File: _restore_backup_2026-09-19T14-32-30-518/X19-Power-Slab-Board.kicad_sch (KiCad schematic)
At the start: 33 parts, among them J2 796636-6, J3 Conn_01x02_Pin, J4 Conn_01x04_Pin, J5 Conn_01x04_Pin, Q1 TSM340N06CP_ROG, U2 MIC5504-3.3YM5-TR, U3 INA237AIDGSR, U4 TMP1075NDRLR, U6 TCAN1044AVDRQ1

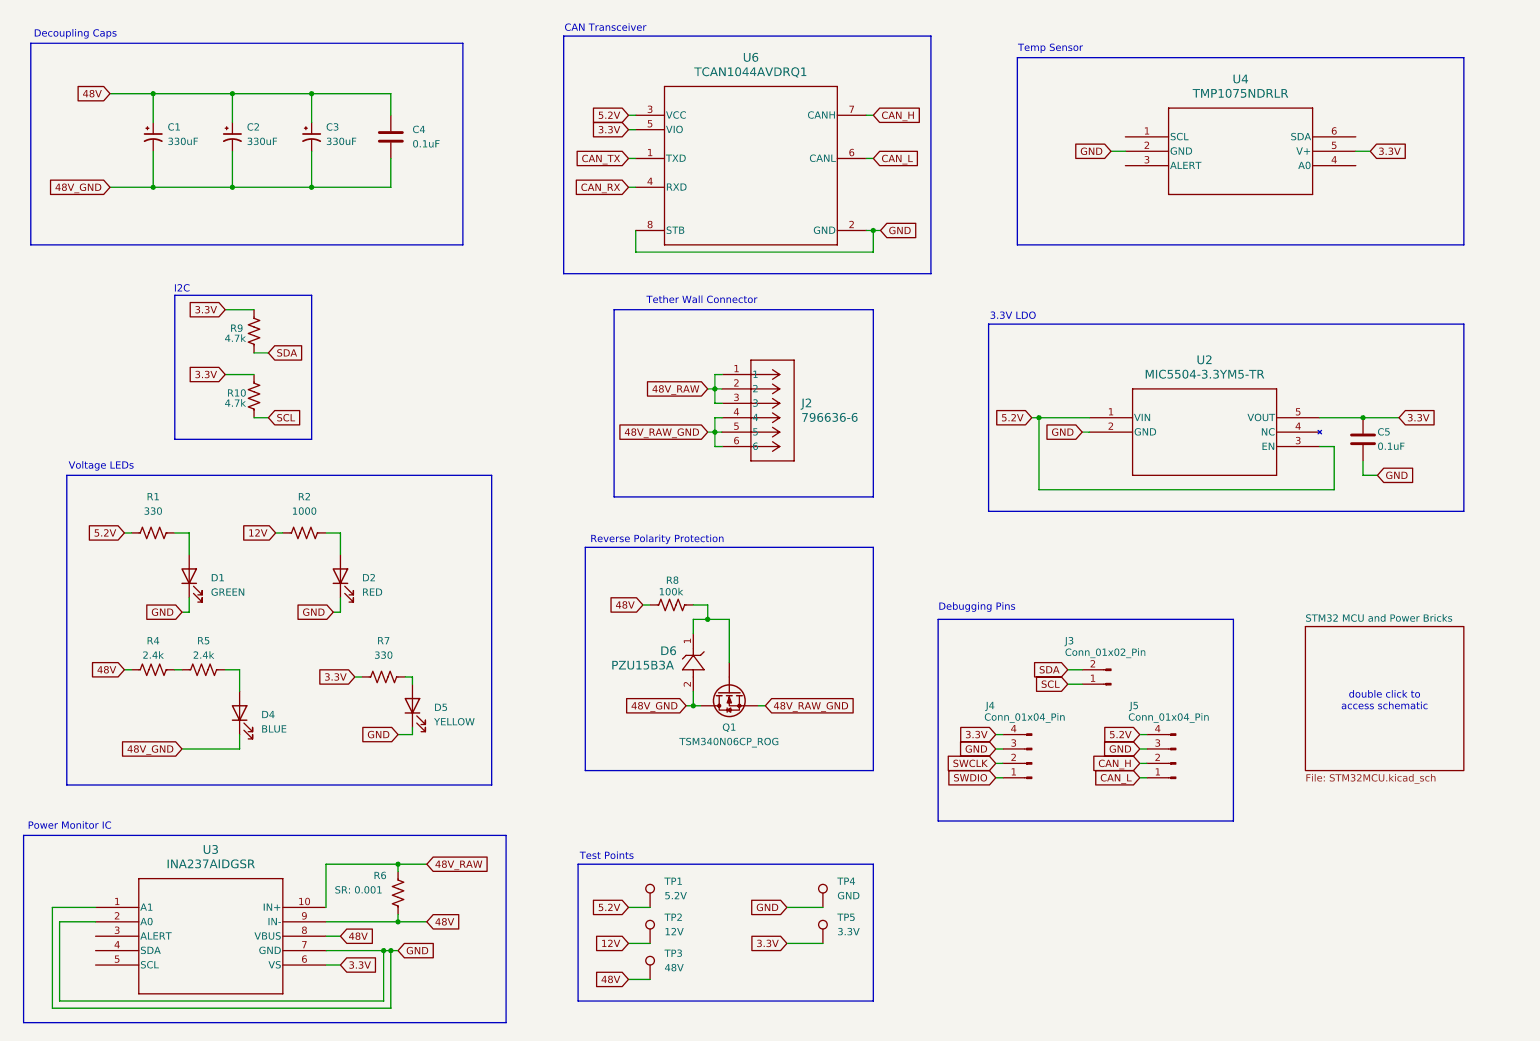
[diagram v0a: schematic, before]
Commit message: added 48-12V bricks
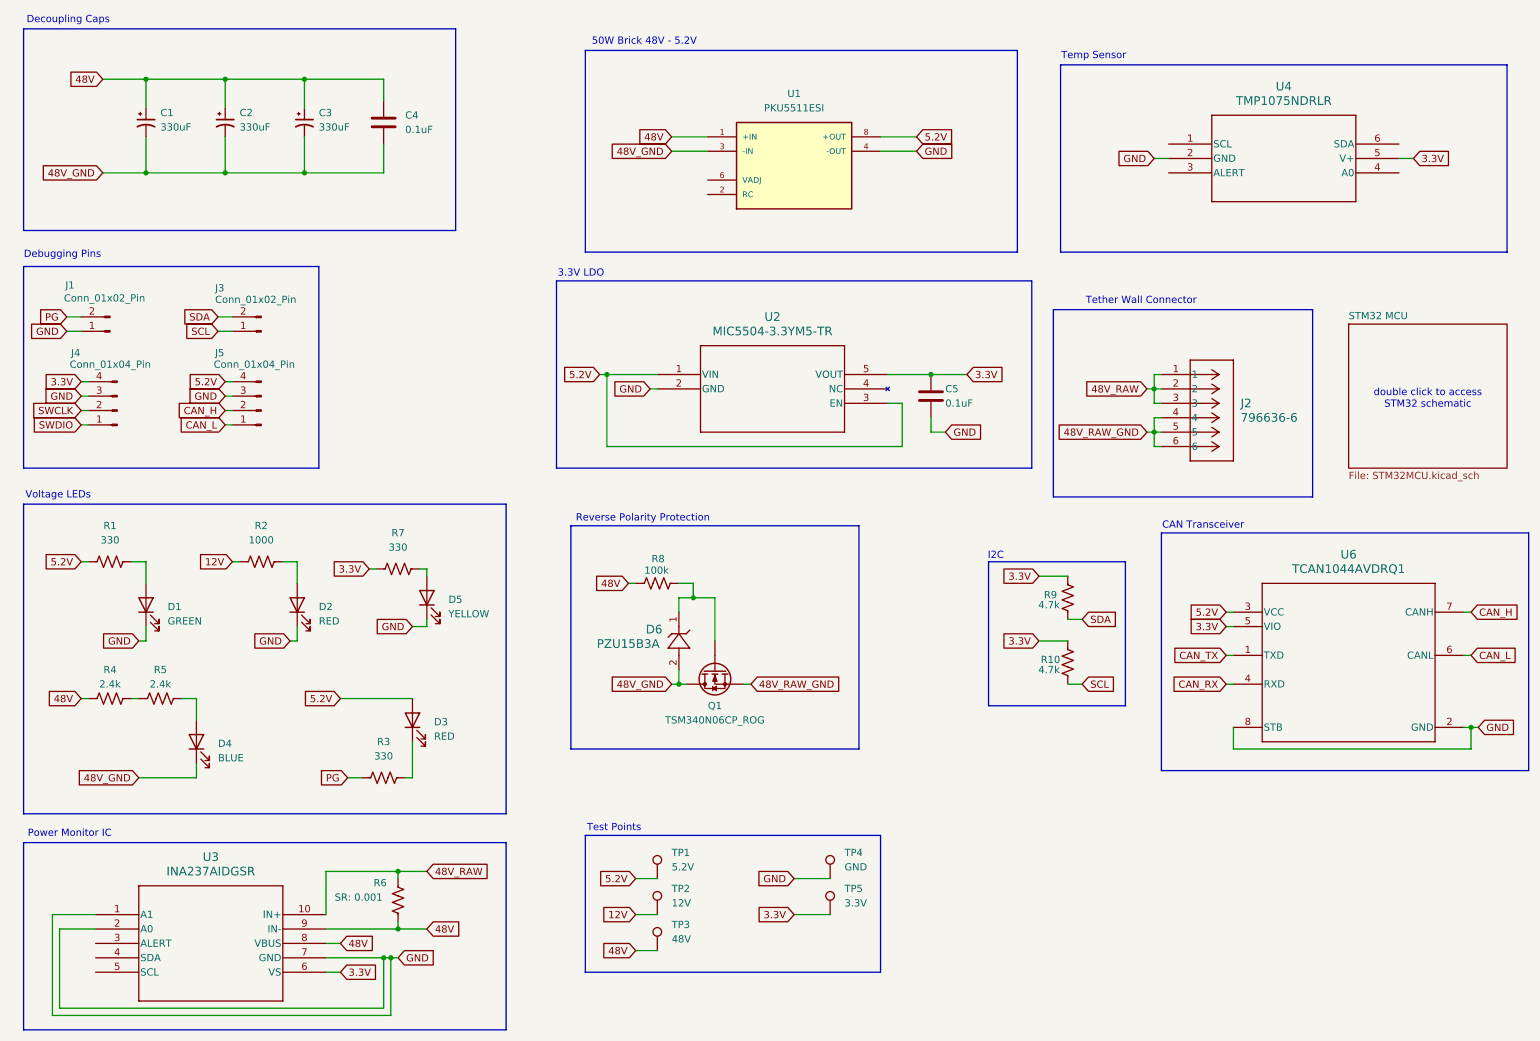
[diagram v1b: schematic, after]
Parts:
- added D3: RED, symbol Device:LED
- added J1: Conn_01x02_Pin, symbol Connector:Conn_01x02_Pin
- added R3: 330, symbol Device:R_US
- added U1: PKU5511ESI, PKU5511ESI:CONV_PKU5511ESI, symbol PKU5511ESI:PKU5511ESI
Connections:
- net 48V: now also U1.1 (+IN)
- net 48V_GND: now also U1.3 (-IN)
- net 5.2V: now also D3.2 (A), U1.8 (+OUT)
- net GND: now also J1.1 (Pin_1), U1.4 (-OUT)
- new net: D3.1 (K), R3.2
- new net PG: J1.2 (Pin_2), R3.1
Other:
- sheet STM32 MCU and Power Bricks renamed STM32 MCU
- note added: "50W Brick 48V - 5.2V"
- note added: "double click to access STM32 schematic"
- note removed: "double click to access schematic"
- moved on the sheet: C1, C2, C3, C4, C5, D1, D2, D4, D5, D6, J2, J3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
